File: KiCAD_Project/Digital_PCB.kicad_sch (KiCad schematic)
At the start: 40 parts, among them J1 NP_Conn_01x02_Relief, J2 Board to Board, J3 1-0001156, J4 1-0001205, J5 1-0001156, J6 NP_Conn_01x04, J7 NP_Conn_01x02_Relief, J8 NP_Conn_01x04, U1 1-0000207, Y1 1-0000721

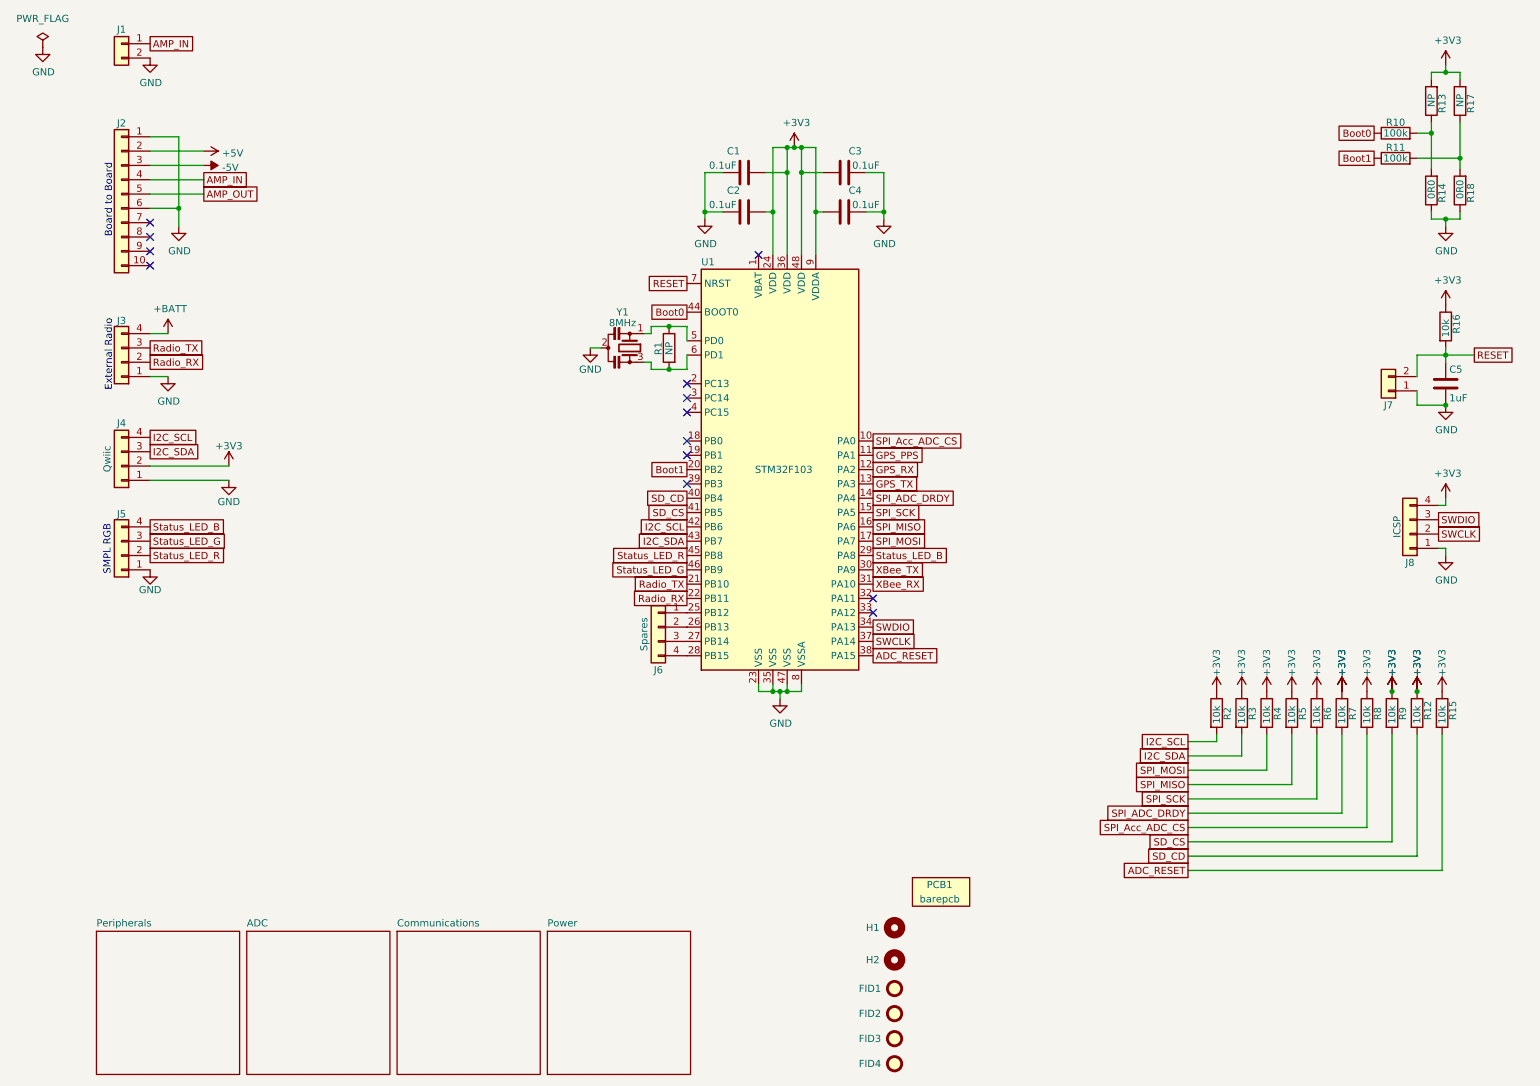
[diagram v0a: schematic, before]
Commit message: Rev 2.1 Changes: - Fixed Issue #11 (U4 Footprint pin 1 indicator) - Added Open Log Header for breakout - Removed SD Circuit - Connected GPS to I2C - Updated IPN and Revision Number
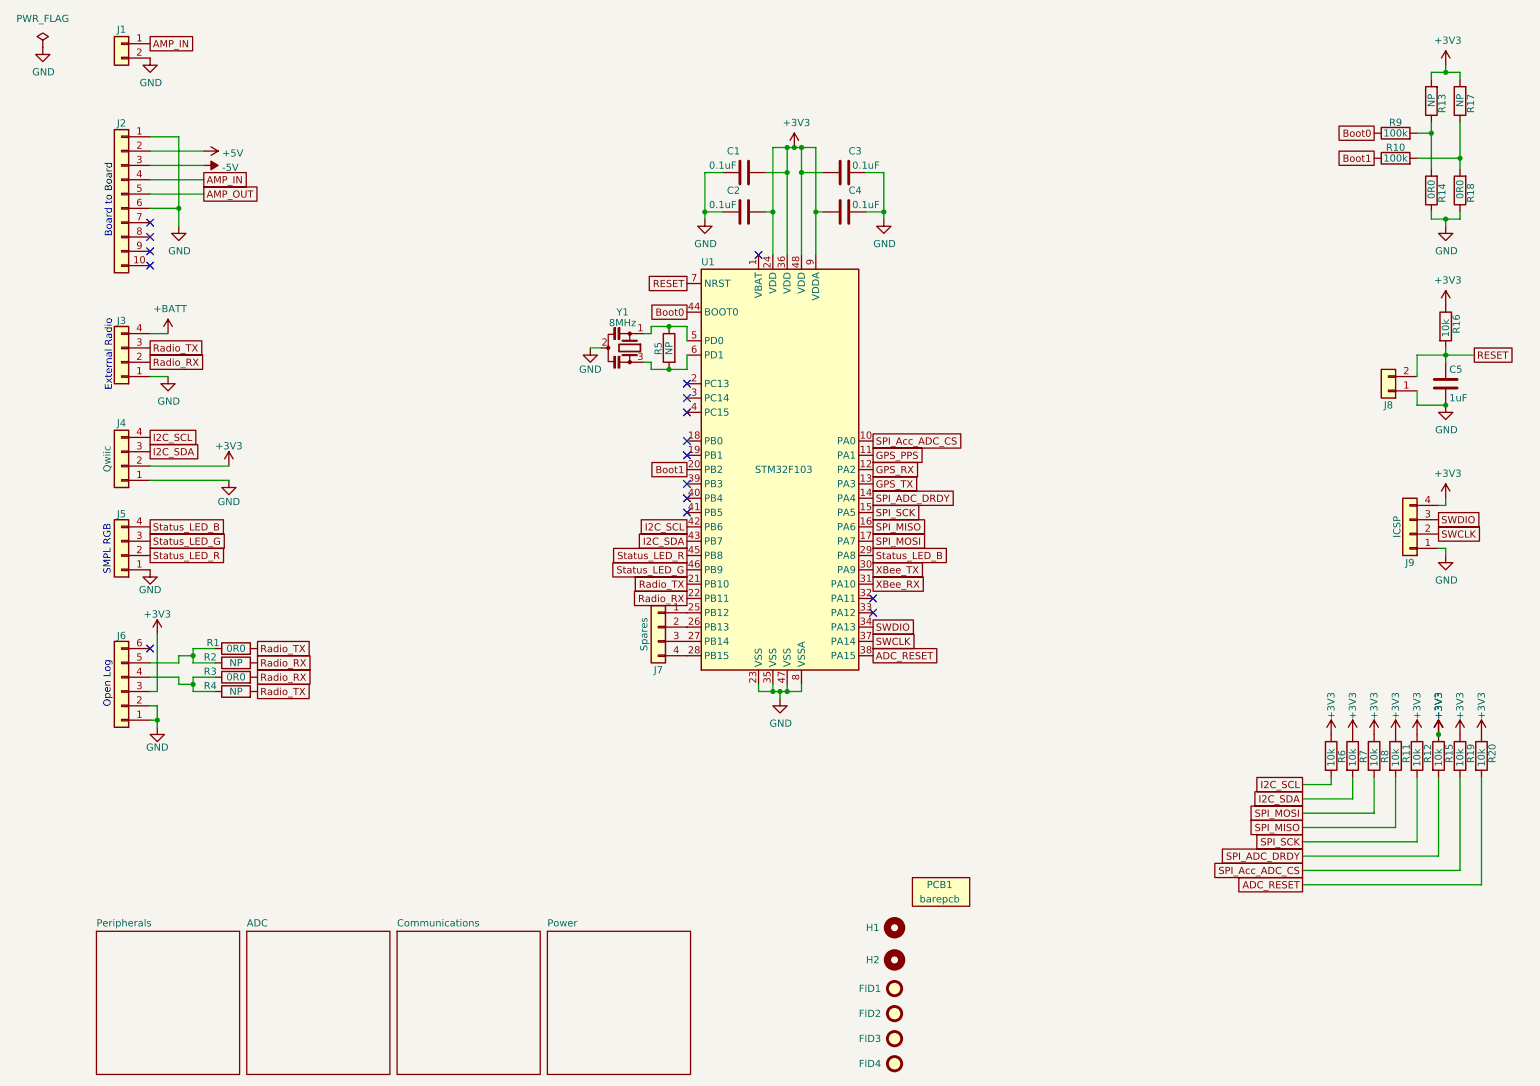
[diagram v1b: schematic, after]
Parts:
- removed R12, R9: 1-0000010, resistors_0603:1-0000010, symbol resistors_0603:1-0000010
- added J6: NP_Conn_01x06, np_connectors:PinHeader_1x06_P2.54mm_Vertical, symbol np_connectors:NP_Conn_01x06
- added R1, R2, R3, R4: 1-0000006, resistors_0603:1-0000006, symbol resistors_0603:1-0000006
- PCB1: Internal Part Number 3-0000270 -> 3-0000279
- renumbered J6 to J7, J7 to J8, J8 to J9, R11 to R10, R5 to R11, R6 to R12, R7 to R15, R8 to R19, R15 to R20, R1 to R5, R2 to R6, R3 to R7, R4 to R8, R10 to R9
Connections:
- net +3V3: now also J6.3 (Pin_3)
- net GND: now also J6.1 (Pin_1), J6.2 (Pin_2)
- net Radio_RX: now also R2.2, R3.2
- net Radio_TX: now also R1.2, R4.2
- net SD_CD: no longer names the net of U1.40 (PB4)
- net SD_CS: no longer names the net of U1.41 (PB5)
- new net: J6.4 (Pin_4), R3.1, R4.1
- new net: J6.5 (Pin_5), R1.1, R2.1
- no-connect marks 13 -> 16
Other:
- note added: "Open Log"
- moved on the sheet: R11, R12, R15, R19, R20, R6, R7, R8
